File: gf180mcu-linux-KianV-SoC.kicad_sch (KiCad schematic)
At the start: 64 parts, among them CN1 HC-PBB40C-70DS-0.4V-2.0-02_CU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, J1 Micro_SD_Card, J2 Conn_01x06_Pin, J3 Conn_01x06_Pin, J4 Conn_02x06_Top_Bottom_custom, J5 USB_C_Receptacle_PowerOnly_6P, SW1 SW_Push, U1 MT48LC16M16A2P, U2 TPS3808DBV, U3 TLV62569DBV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

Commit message: kicad: fix capacitor footprints + add GND stitching vias
Switch C1/C3/C28 from resistor footprints to proper 0603 capacitor footprints (C1 to JLCPCB lib + 3D model)

Tweak pad sizes/placement + silkscreen/ref visibility

Add additional GND vias for stitching and minor route/via coordinate cleanup
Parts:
- C1: footprint Resistor_SMD:R_0603_1608Metric -> PCM_JLCPCB:C_0603
- C28, C3: footprint Resistor_SMD:R_0603_1608Metric -> Capacitor_SMD:C_0603_1608Metric
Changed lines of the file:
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@@
 			)
 		)
-		(property "Footprint" "Resistor_SMD:R_0603_1608Metric"
+		(property "Footprint" "Capacitor_SMD:C_0603_1608Metric"
 			(at 494.9952 66.04 0)
 			(effects
@@
 			)
 		)
-		(property "Footprint" "Resistor_SMD:R_0603_1608Metric"
+		(property "Footprint" "Capacitor_SMD:C_0603_1608Metric"
 			(at 54.3052 213.36 0)
 			(effects
@@
 			)
 		)
-		(property "Footprint" "Resistor_SMD:R_0603_1608Metric"
+		(property "Footprint" "PCM_JLCPCB:C_0603"
 			(at 42.8752 213.36 0)
 			(effects

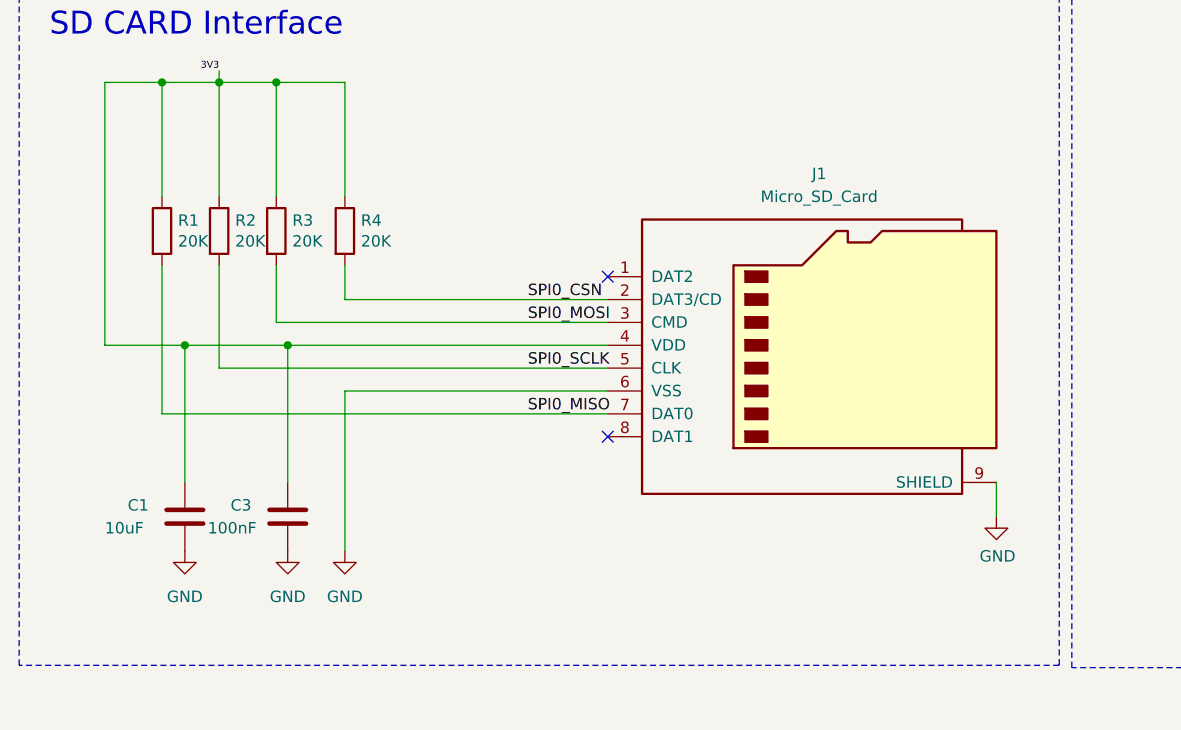
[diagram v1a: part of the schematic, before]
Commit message: pcb: DFM cleanup, SD card footprint update, oscillator fixes
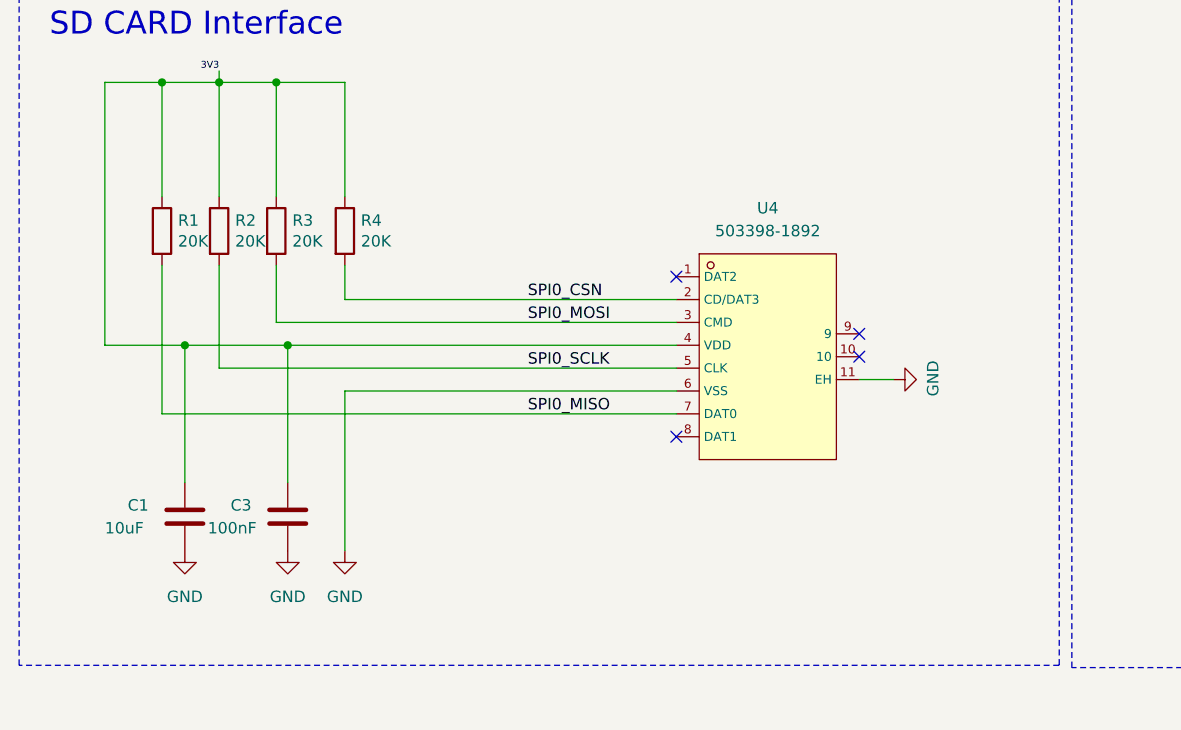
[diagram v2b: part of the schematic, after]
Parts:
- removed J1: Micro_SD_Card, Connector_Card:microSD_HC_Molex_47219-2001, symbol Connector:Micro_SD_Card
- added U4: 503398-1892, footprint:TF-SMD_503398-1892, symbol 503398-1892:503398-1892
- CN1: Field (none) -> LCSC C19089262
- U2: Field5 (none) -> LCSC C189211
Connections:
- net 3V3: now also U4.4 (VDD)
- net GND: now also U4.11 (EH), U4.6 (VSS)
- net SPI0_CSN: now also U4.2 (CD/DAT3)
- net SPI0_MISO: now also U4.7 (DAT0)
- net SPI0_MOSI: now also U4.3 (CMD)
- net SPI0_SCLK: now also U4.5 (CLK)
- no-connect marks 8 -> 10
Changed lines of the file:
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@@
 	)
 	(no_connect
-		(at 354.33 100.33)
+		(at 96.52 200.66)
+	)
+	(no_connect
+		(at 96.52 182.88)
 	)
 	(no_connect
-		(at 88.9 182.88)
+		(at 354.33 100.33)
 	)
 	(no_connect
-		(at 88.9 200.66)
+		(at 116.84 191.77)
 	)
 	(no_connect
 		(at 320.04 210.82)
 	)
+	(no_connect
+		(at 116.84 189.23)
+	)
 	(wire
 		(pts
@@
 	(wire
 		(pts
-			(xy 132.08 205.74) (xy 132.08 209.55)
+			(xy 116.84 194.31) (xy 120.65 194.31)
 		)
 		(stroke
@@
 	(wire
 		(pts
-			(xy 45.72 193.04) (xy 88.9 193.04)
+			(xy 45.72 193.04) (xy 96.52 193.04)
 		)
 		(stroke
@@
 	(wire
 		(pts
-			(xy 39.37 198.12) (xy 88.9 198.12)
+			(xy 39.37 198.12) (xy 96.52 198.12)
 		)
 		(stroke
@@
 	(wire
 		(pts
-			(xy 53.34 190.5) (xy 88.9 190.5)
+			(xy 53.34 190.5) (xy 96.52 190.5)
 		)
 		(stroke
@@
 	(wire
 		(pts
-			(xy 59.69 185.42) (xy 88.9 185.42)
+			(xy 59.69 185.42) (xy 96.52 185.42)
 		)
 		(stroke
@@
 	(wire
 		(pts
-			(xy 52.07 187.96) (xy 88.9 187.96)
+			(xy 52.07 187.96) (xy 96.52 187.96)
 		)
 		(stroke
@@
 	(wire
 		(pts
-			(xy 59.69 195.58) (xy 88.9 195.58)
+			(xy 59.69 195.58) (xy 96.52 195.58)
 		)
 		(stroke
@@
 	)
 	(symbol
+		(lib_id "503398-1892:503398-1892")
+		(at 106.68 191.77 0)
+		(unit 1)
+		(exclude_from_sim no)
+		(in_bom yes)
+		(on_board yes)
+		(dnp no)
+		(fields_autoplaced yes)
+		(property "Reference" "U4"
+			(at 106.68 175.26 0)
+			(effects
+				(font
+					(size 1.27 1.27)
+				)
+			)
+		)
+		(property "Value" "503398-1892"
+			(at 106.68 177.8 0)
+			(effects
+				(font
+					(size 1.27 1.27)
+				)
+			)
+		)
+		(property "Footprint" "footprint:TF-SMD_503398-1892"
+			(at 106.68 201.93 0)
+			(effects
+				(font
+					(size 1.27 1.27)
+					(italic yes)
+				)
+				(hide yes)
+			)
+		)
+		(property "Datasheet" "https://item.szlcsc.com/423383.html"
+			(at 104.394 191.643 0)
+			(effects
+				(font
+					(size 1.27 1.27)
+				)
+				(justify left)
+				(hide yes)
+			)
+		)
+		(property "Description" ""
+			(at 106.68 191.77 0)
+			(effects
+				(font
+					(size 1.27 1.27)
+				)
+				(hide yes)
+			)
+		)
+		(property "LCSC" "C428492"
+			(at 106.68 191.77 0)
+			(effects
+				(font
+					(size 1.27 1.27)
+				)
+				(hide yes)
+			)
+		)
+		(pin "5"
+		)
+		(pin "1"
+		)
+		(pin "4"
+		)
+		(pin "10"
+		)
+		(pin "2"
+		)
+		(pin "6"
+		)
+		(pin "8"
+		)
+		(pin "9"
+		)
+		(pin "3"
+		)
+		(pin "11"
+		)
+		(pin "7"
+		)
+		(instances
+			(project ""
+				(path "/b49541e6-dc9c-47ff-bd25-504a2faaf33a"
+					(reference "U4")
+					(unit 1)
+				)
+			)
+		)
+	)
+	(symbol
 		(lib_id "Device:C")
 		(at 95.25 124.46 180)
@@
 	(symbol
 		(lib_id "power:GND")
-		(at 132.08 209.55 0)
+		(at 120.65 194.31 90)
 		(unit 1)
 		(exclude_from_sim no)
@@
 		(dnp no)
 		(property "Reference" "#PWR013"
-			(at 132.08 215.9 0)
+			(at 127 194.31 0)
 			(effects
 				(font
@@
 		)
 		(property "Value" "GND"
-			(at 132.207 213.9442 0)
+			(at 125.0442 194.183 0)
 			(effects
 				(font
@@
 		)
 		(property "Footprint" ""
-			(at 132.08 209.55 0)
+			(at 120.65 194.31 0)
 			(effects
 				(font
@@
 		)
 		(property "Datasheet" ""
-			(at 132.08 209.55 0)
+			(at 120.65 194.31 0)
 			(effects
 				(font
@@
 		)
 		(property "Description" ""
-			(at 132.08 209.55 0)
+			(at 120.65 194.31 0)
 			(effects
 				(font
@@
 	)
 	(symbol
-		(lib_id "Connector:Micro_SD_Card")
-		(at 111.76 190.5 0)
-		(unit 1)
-		(exclude_from_sim no)
-		(in_bom yes)
-		(on_board yes)
-		(dnp no)
-		(fields_autoplaced yes)
-		(property "Reference" "J1"
-			(at 112.395 171.45 0)
-			(effects
-				(font
-					(size 1.27 1.27)
-				)
-			)
-		)
-		(property "Value" "Micro_SD_Card"
-			(at 112.395 173.99 0)
-			(effects
-				(font
-					(size 1.27 1.27)
-				)
-			)
-		)
-		(property "Footprint" "Connector_Card:microSD_HC_Molex_47219-2001"
-			(at 140.97 182.88 0)
-			(effects
-				(font
-					(size 1.27 1.27)
-				)
-				(hide yes)
-			)
-		)
-		(property "Datasheet" "https://www.we-online.com/components/products/datasheet/693072010801.pdf"
-			(at 111.76 190.5 0)
-			(effects
-				(font
-					(size 1.27 1.27)
-				)
-				(hide yes)
-			)
-		)
-		(property "Description" "Micro SD Card Socket"
-			(at 111.76 190.5 0)
-			(effects
-				(font
-					(size 1.27 1.27)
-				)
-				(hide yes)
-			)
-		)
-		(pin "4"
-		)
-		(pin "5"
-		)
-		(pin "3"
-		)
-		(pin "6"
-		)
-		(pin "7"
-		)
-		(pin "9"
-		)
-		(pin "8"
-		)
-		(pin "2"
-		)
-		(pin "1"
-		)
-		(instances
-			(project ""
-				(path "/b49541e6-dc9c-47ff-bd25-504a2faaf33a"
-					(reference "J1")
-					(unit 1)
-				)
-			)
-		)
-	)
-	(symbol
 		(lib_id "power:GND")
 		(at 251.46 134.62 0)
@@
 			)
 		)
+		(property "Field5" "LCSC    C189211"
+			(at 238.76 115.57 0)
+			(effects
+				(font
+					(size 1.27 1.27)
+				)
+				(hide yes)
+			)
+		)
 		(pin "2"
 		)
@@
 			(effects
 				(font
+					(size 1.27 1.27)
+				)
+				(hide yes)
+			)
+		)
+		(property "Field" "LCSC  C19089262"
+			(at 182.88 118.11 0)
+			(effects
+				(font

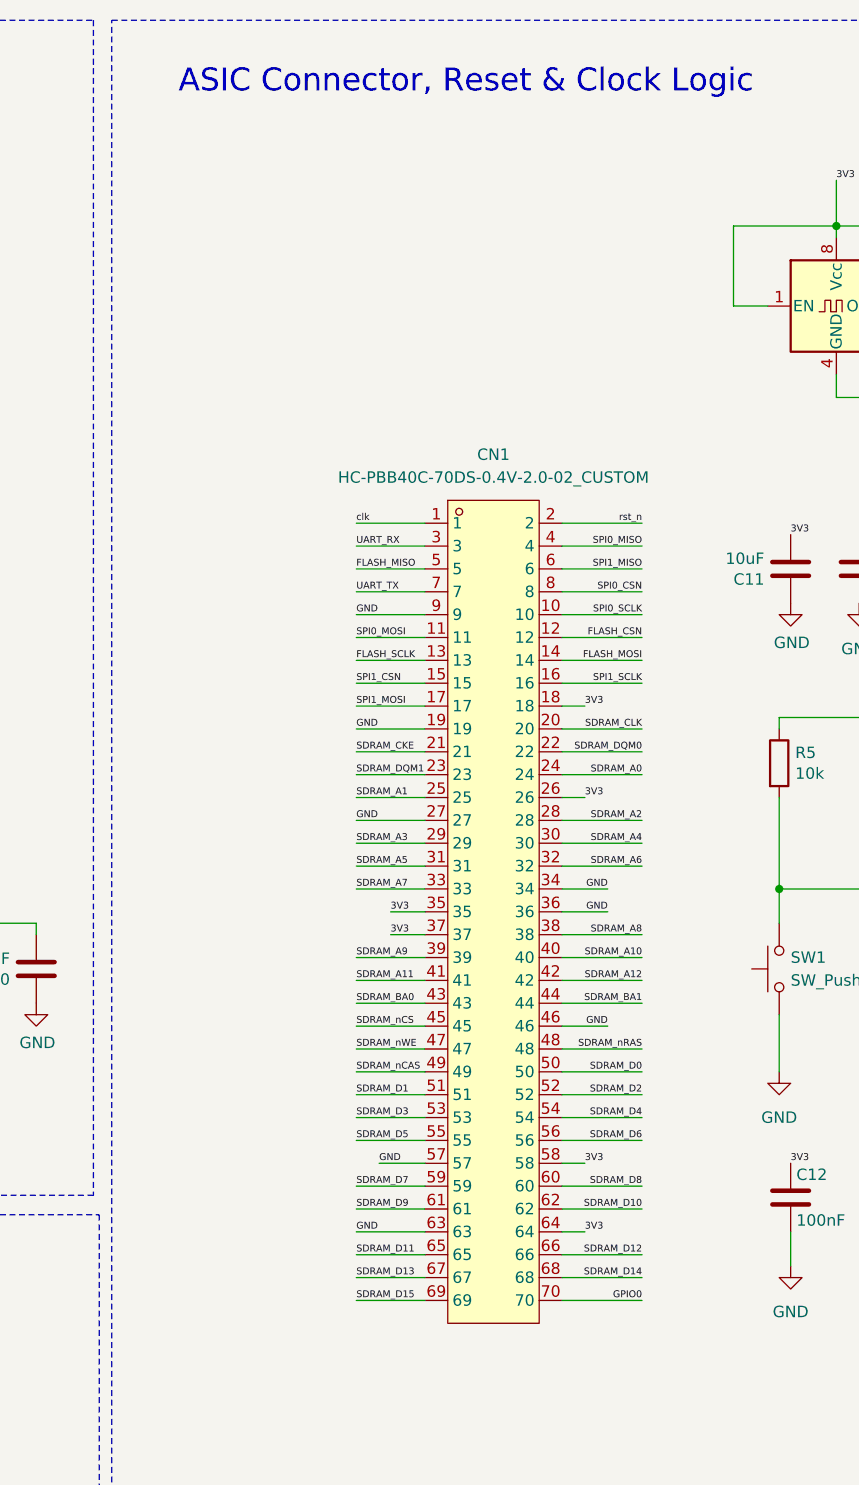
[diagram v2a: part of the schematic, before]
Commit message: update connector assigments and reroute
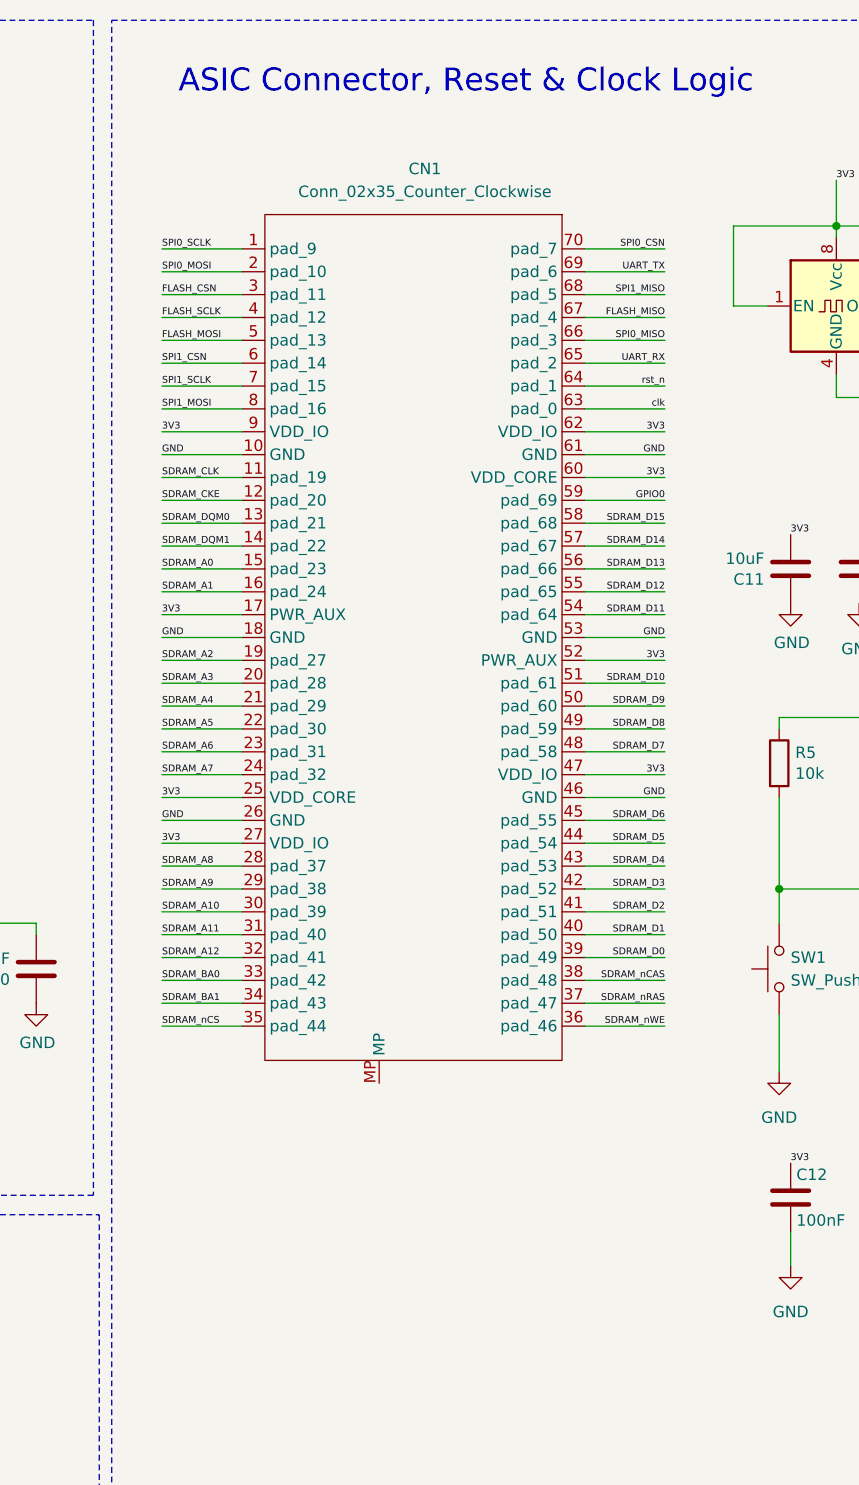
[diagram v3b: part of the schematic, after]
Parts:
- removed CN1: HC-PBB40C-70DS-0.4V-2.0-02_CUSTOM, C19089262:CONN-SMD_70P-P0.40_HC-PBB40C-70DS-0.4V-3.0-02, symbol New_Library:HC-PBB40C-70DS-0.4V-2.0-02_CUSTOM
- added CN1: Conn_02x35_Counter_Clockwise, LD-CONNECTORS:CONN-SMD_70P-P0.40_HC-PBB40C-70DS-0.4V-3.0-02, symbol WaferSpace:70pin_ws_default_mezzanine_motherboard
- FB1: value ~ -> (none)
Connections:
- net 3V3: now also CN1.17 (PWR_AUX), CN1.25 (VDD_CORE), CN1.27 (VDD_IO), CN1.47 (VDD_IO), CN1.52 (PWR_AUX), CN1.60 (VDD_CORE), CN1.62 (VDD_IO), CN1.9 (VDD_IO)
- net FLASH_CSN: now also CN1.3 (pad_11)
- net FLASH_MISO: now also CN1.67 (pad_4)
- net FLASH_MOSI: now also CN1.5 (pad_13)
- net FLASH_SCLK: now also CN1.4 (pad_12)
- net GND: now also CN1.10 (GND), CN1.18 (GND), CN1.26 (GND), CN1.46 (GND), CN1.53 (GND), CN1.61 (GND)
- net GPIO0: now also CN1.59 (pad_69)
- net SDRAM_A0: now also CN1.15 (pad_23)
- net SDRAM_A1: now also CN1.16 (pad_24)
- net SDRAM_A10: now also CN1.30 (pad_39)
- net SDRAM_A11: now also CN1.31 (pad_40)
- net SDRAM_A12: now also CN1.32 (pad_41)
- net SDRAM_A2: now also CN1.19 (pad_27)
- net SDRAM_A3: now also CN1.20 (pad_28)
- net SDRAM_A4: now also CN1.21 (pad_29)
- net SDRAM_A5: now also CN1.22 (pad_30)
- net SDRAM_A6: now also CN1.23 (pad_31)
- net SDRAM_A7: now also CN1.24 (pad_32)
- net SDRAM_A8: now also CN1.28 (pad_37)
- net SDRAM_A9: now also CN1.29 (pad_38)
- net SDRAM_BA0: now also CN1.33 (pad_42)
- net SDRAM_BA1: now also CN1.34 (pad_43)
- net SDRAM_CKE: now also CN1.12 (pad_20)
- net SDRAM_CLK: now also CN1.11 (pad_19)
- net SDRAM_D0: now also CN1.39 (pad_49)
- net SDRAM_D1: now also CN1.40 (pad_50)
- net SDRAM_D10: now also CN1.51 (pad_61)
- net SDRAM_D11: now also CN1.54 (pad_64)
- net SDRAM_D12: now also CN1.55 (pad_65)
- net SDRAM_D13: now also CN1.56 (pad_66)
- net SDRAM_D14: now also CN1.57 (pad_67)
- net SDRAM_D15: now also CN1.58 (pad_68)
- net SDRAM_D2: now also CN1.41 (pad_51)
- net SDRAM_D3: now also CN1.42 (pad_52)
- net SDRAM_D4: now also CN1.43 (pad_53)
- net SDRAM_D5: now also CN1.44 (pad_54)
- net SDRAM_D6: now also CN1.45 (pad_55)
- net SDRAM_D7: now also CN1.48 (pad_58)
- net SDRAM_D8: now also CN1.49 (pad_59)
- net SDRAM_D9: now also CN1.50 (pad_60)
- net SDRAM_DQM0: now also CN1.13 (pad_21)
- net SDRAM_DQM1: now also CN1.14 (pad_22)
- net SDRAM_nCAS: now also CN1.38 (pad_48)
- net SDRAM_nCS: now also CN1.35 (pad_44)
- net SDRAM_nRAS: now also CN1.37 (pad_47)
- net SDRAM_nWE: now also CN1.36 (pad_46)
- net SPI0_CSN: now also CN1.70 (pad_7)
- net SPI0_MISO: now also CN1.66 (pad_3)
- net SPI0_MOSI: now also CN1.2 (pad_10)
- net SPI0_SCLK: now also CN1.1 (pad_9)
- net SPI1_CSN: now also CN1.6 (pad_14)
- net SPI1_MISO: now also CN1.68 (pad_5)
- net SPI1_MOSI: now also CN1.8 (pad_16)
- net SPI1_SCLK: now also CN1.7 (pad_15)
- net UART_RX: now also CN1.65 (pad_2)
- net UART_TX: now also CN1.69 (pad_6)
- net clk: now also CN1.63 (pad_0)
- net rst_n: now also CN1.64 (pad_1)

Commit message: Set C24 to 4.7uF
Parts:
- C24: value 22uF -> 4.7uF; MPN CC0805ZKY5V5BB226 -> (none)
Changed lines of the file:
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@@
 			)
 		)
-		(property "Value" "22uF"
+		(property "Value" "4.7uF"
 			(at 424.815 119.38 0)
 			(show_name no)
@@
 			(show_name no)
 			(do_not_autoplace no)
-			(effects
-				(font
-					(size 1.27 1.27)
-				)
-			)
-		)
-		(property "MPN" "CC0805ZKY5V5BB226 "
-			(at 424.18 116.84 0)
-			(hide yes)
-			(show_name no)
-			(do_not_autoplace no)
